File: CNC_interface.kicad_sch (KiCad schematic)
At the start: 27 parts, among them J1 Conn_01x04_Male, J10 Conn_01x08, J11 Conn_01x08, J12 Conn_01x08, J13 Conn_01x08, J14 Conn_01x03_Male, J15 Conn_01x03_Male, J16 Conn_01x03_Male, J17 Conn_01x08, J18 Conn_01x10, J19 USB_C_Receptacle, J2 Conn_01x04_Male, J3 Conn_01x04_Male, J5 Screw_Terminal_01x02, J6 Screw_Terminal_01x02, J8 Conn_01x08, J9 Conn_01x08, Q1 Q_NMOS_GDS, U4 LM2596S-5

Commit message: Starting routing & adding capa
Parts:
- added C3, C4, C5: C_Polarized, symbol Device:C_Polarized
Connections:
- net GND is gone; now on net +5V: C1.2, C2.2, D2.2 (A), J10.1 (Pin_1), J10.7 (Pin_7), J12.1 (Pin_1), J12.7 (Pin_7), J14.2 (Pin_2), J15.2 (Pin_2), J16.2 (Pin_2), J18.4 (Pin_4), J19.A1 (GND), J19.A12 (GND), J19.B1 (GND), J19.B12 (GND), J19.S1 (SHIELD), J5.2 (Pin_2), J8.1 (Pin_1), J8.7 (Pin_7), Q1.3 (S), R1.2, U4.3 (GND), U4.5 (~{ON}/OFF)
- net +5V: now also C3.1, C3.2, C4.1, C4.2, C5.1, C5.2
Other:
- moved on the sheet: J10, J11, J12, J13

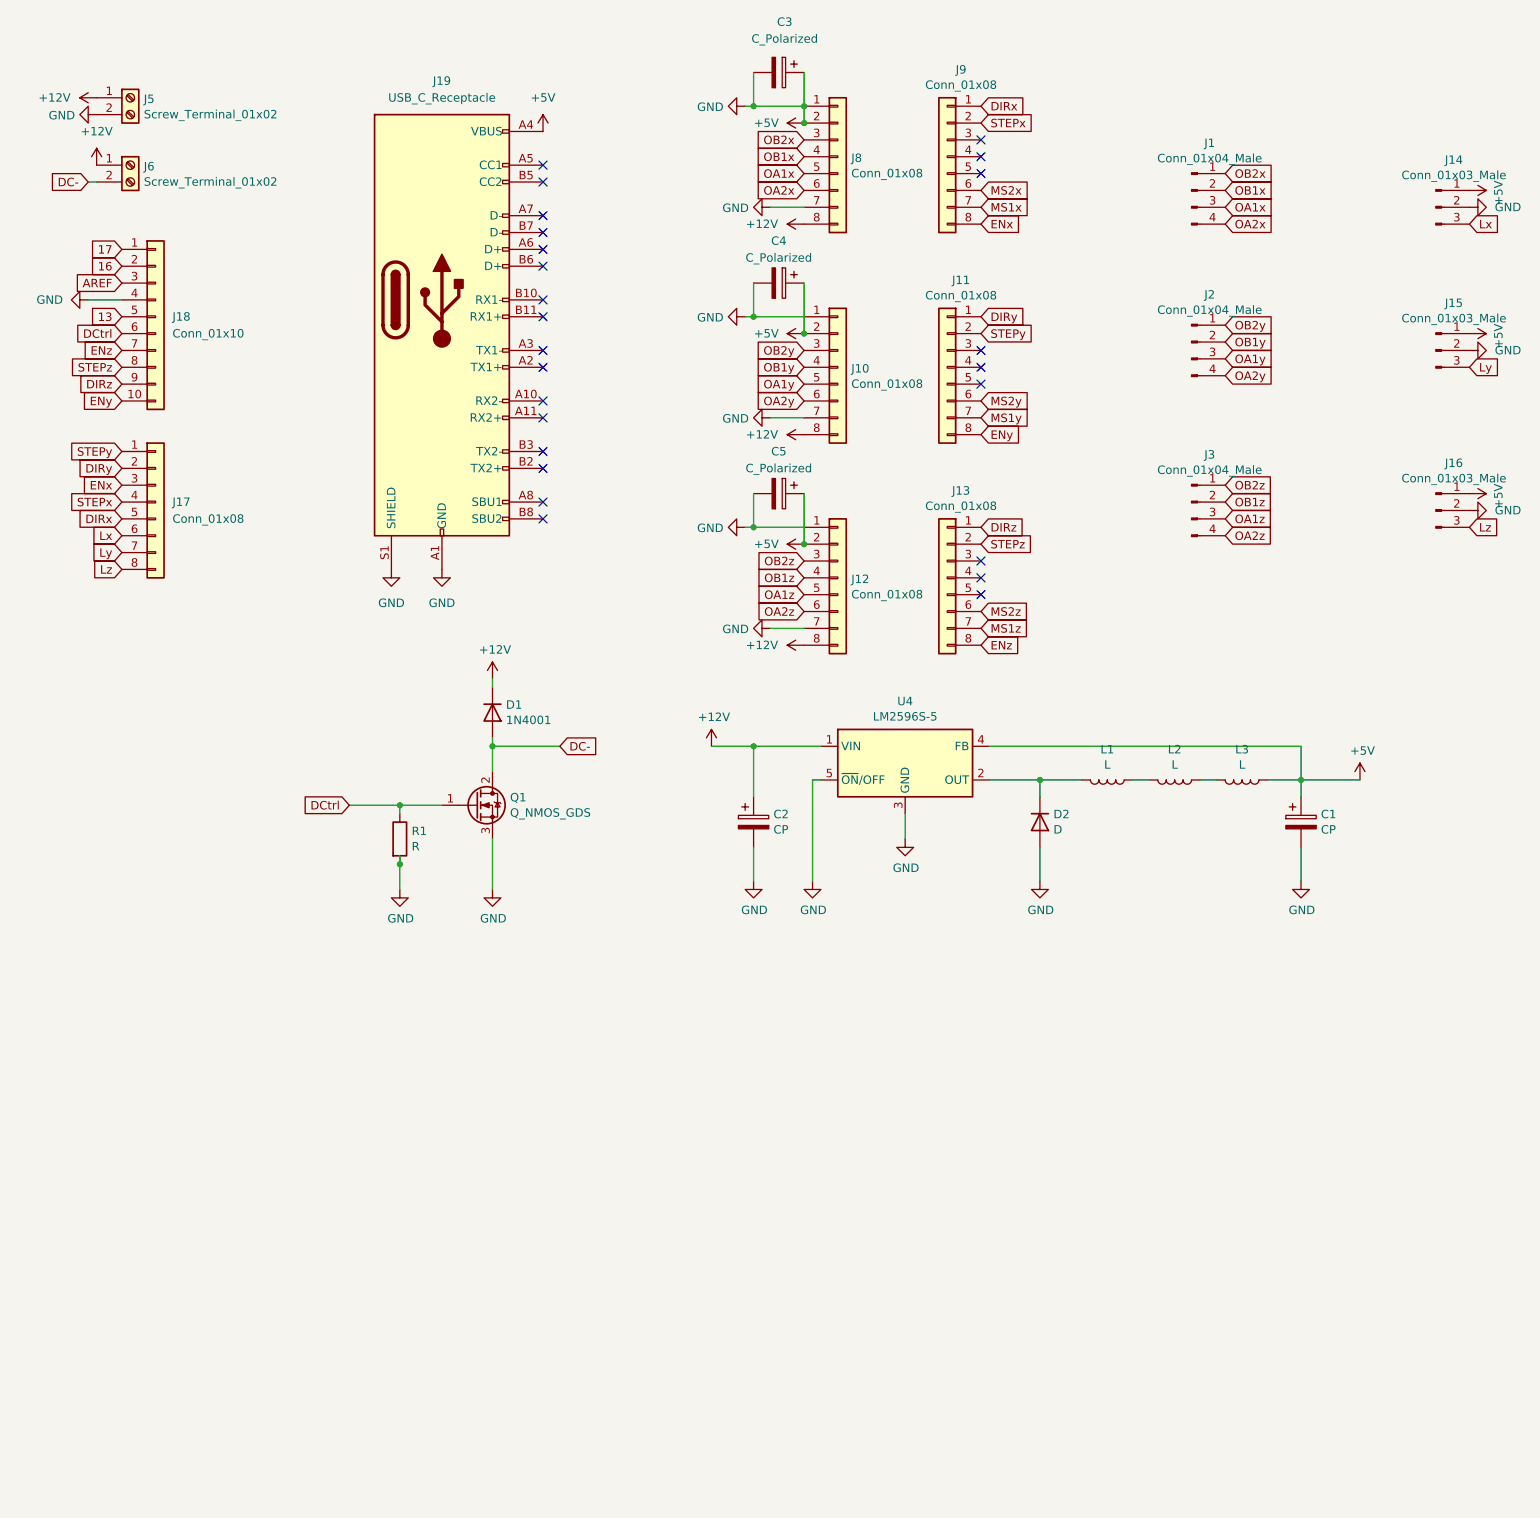
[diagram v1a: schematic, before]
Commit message: Add 12V power stage
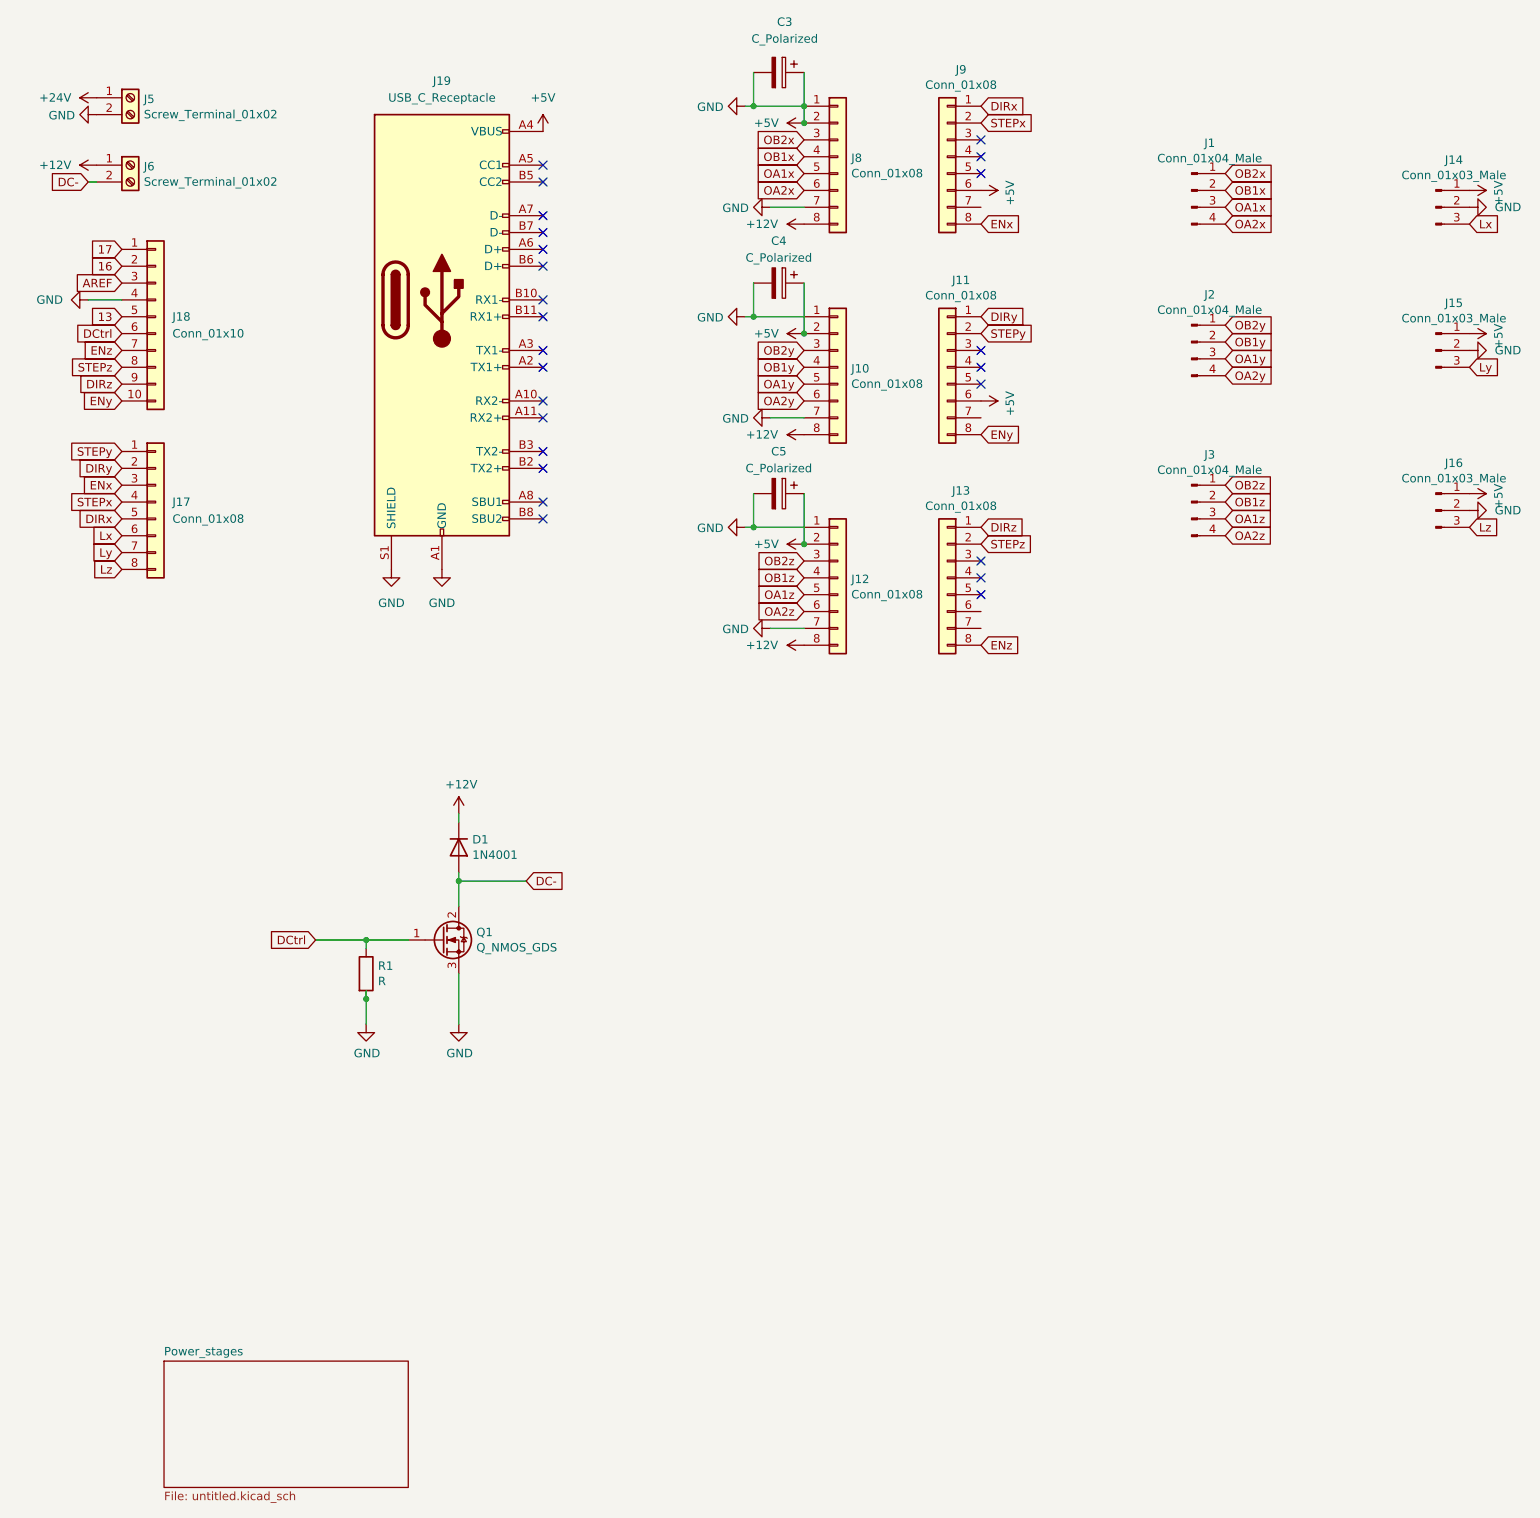
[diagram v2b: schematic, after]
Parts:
- removed C1: CP, Capacitor_THT:CP_Radial_D8.0mm_P3.50mm, symbol Device:CP
- removed C2: CP, Capacitor_THT:CP_Radial_D10.0mm_P5.00mm, symbol Device:CP
- removed D2: D, Diode_THT:D_DO-201AD_P15.24mm_Horizontal, symbol Device:D
- removed L1, L2, L3: L, Inductor_SMD:L_TDK_SLF10145, symbol Device:L
- removed U4: LM2596S-5, Package_TO_SOT_SMD:TO-263-5_TabPin3, symbol Regulator_Switching:LM2596S-5
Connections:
- net MS2x is gone; now on net +5V: J9.6 (Pin_6)
- net MS2y is gone; now on net +5V: J11.6 (Pin_6)
- net +12V: no longer J5.1 (Pin_1)
- net MS1x: no longer names the net of J9.7 (Pin_7)
- net MS1y: no longer names the net of J11.7 (Pin_7)
- net MS1z: no longer names the net of J13.7 (Pin_7)
- net MS2z: no longer names the net of J13.6 (Pin_6)
- new net +24V: J5.1 (Pin_1)
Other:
- added sheet Power_stages (untitled.kicad_sch)
- moved on the sheet: D1, Q1, R1

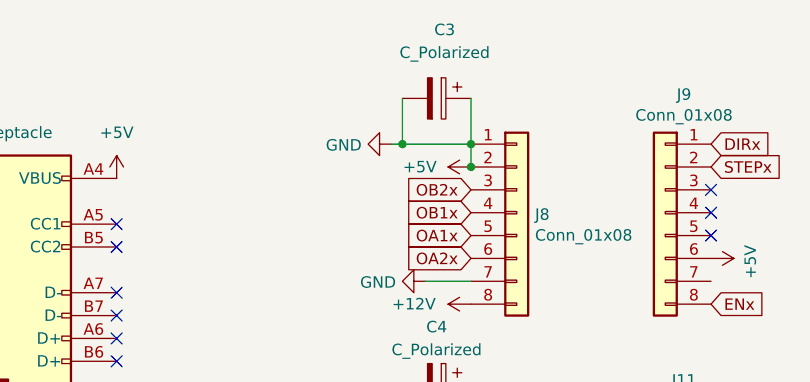
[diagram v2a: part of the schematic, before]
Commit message: delete the short circuit
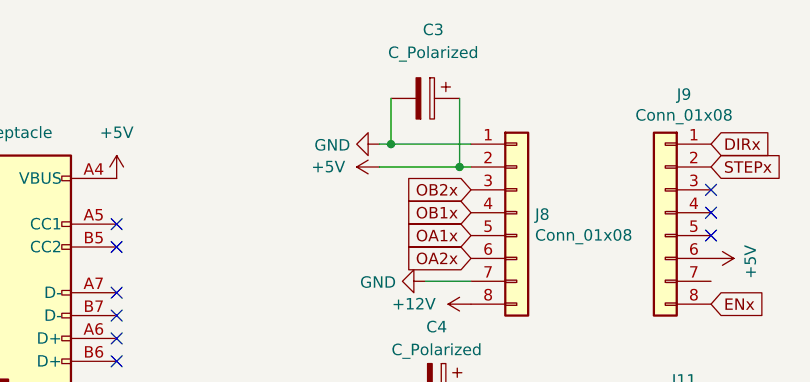
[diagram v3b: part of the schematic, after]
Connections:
- net +5V: no longer C3.2, C4.2, C5.2, J10.1 (Pin_1), J10.7 (Pin_7), J12.1 (Pin_1), J12.7 (Pin_7), J14.2 (Pin_2), J15.2 (Pin_2), J16.2 (Pin_2), J18.4 (Pin_4), J19.A1 (GND), J19.A12 (GND), J19.B1 (GND), J19.B12 (GND), J19.S1 (SHIELD), J5.2 (Pin_2), J8.1 (Pin_1), J8.7 (Pin_7), Q1.3 (S), R1.2
- new net GND: C3.2, C4.2, C5.2, J10.1 (Pin_1), J10.7 (Pin_7), J12.1 (Pin_1), J12.7 (Pin_7), J14.2 (Pin_2), J15.2 (Pin_2), J16.2 (Pin_2), J18.4 (Pin_4), J19.A1 (GND), J19.A12 (GND), J19.B1 (GND), J19.B12 (GND), J19.S1 (SHIELD), J5.2 (Pin_2), J8.1 (Pin_1), J8.7 (Pin_7), Q1.3 (S), R1.2
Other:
- moved on the sheet: C3
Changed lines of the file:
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@@
 (kicad_sch (version 20211123) (generator eeschema)
   (paper "A4")
-  (junction (at 148.59 35.56) (diameter 0) (color 0 0 0 0)
-  )
-  (junction (at 140.97 33.02) (diameter 0) (color 0 0 0 0)
-  )
   (junction (at 148.59 99.06) (diameter 0) (color 0 0 0 0)
   )
@@
   (junction (at 140.97 96.52) (diameter 0) (color 0 0 0 0)
   )
-  (junction (at 148.59 33.02) (diameter 0) (color 0 0 0 0)
+  (junction (at 147.32 35.56) (diameter 0) (color 0 0 0 0)
   )
   (junction (at 82.55 167.64) (diameter 0) (color 0 0 0 0)
+  )
+  (junction (at 139.7 33.02) (diameter 0) (color 0 0 0 0)
   )
   (no_connect (at 175.26 101.6))
@@
   (no_connect (at 109.22 49.53))
   (no_connect (at 109.22 44.45))
-  (wire (pts (xy 139.7 33.02) (xy 140.97 33.02))
+  (wire (pts (xy 138.43 33.02) (xy 139.7 33.02))
     (stroke (width 0) (type default) (color 0 0 0 0))
   )
@@
     (stroke (width 0) (type default) (color 0 0 0 0))
   )
-  (wire (pts (xy 140.97 27.94) (xy 140.97 33.02))
+  (wire (pts (xy 139.7 27.94) (xy 139.7 33.02))
     (stroke (width 0) (type default) (color 0 0 0 0))
   )
@@
     (stroke (width 0) (type default) (color 0 0 0 0))
   )
+  (wire (pts (xy 138.43 35.56) (xy 147.32 35.56))
+    (stroke (width 0) (type default) (color 0 0 0 0))
+  )
   (wire (pts (xy 106.68 149.86) (xy 96.52 149.86))
     (stroke (width 0) (type default) (color 0 0 0 0))
@@
     (stroke (width 0) (type default) (color 0 0 0 0))
   )
-  (wire (pts (xy 148.59 27.94) (xy 148.59 33.02))
-    (stroke (width 0) (type default) (color 0 0 0 0))
-  )
   (wire (pts (xy 140.97 59.69) (xy 140.97 64.77))
     (stroke (width 0) (type default) (color 0 0 0 0))
@@
     (stroke (width 0) (type default) (color 0 0 0 0))
   )
+  (wire (pts (xy 147.32 27.94) (xy 147.32 35.56))
+    (stroke (width 0) (type default) (color 0 0 0 0))
+  )
   (wire (pts (xy 140.97 91.44) (xy 140.97 96.52))
     (stroke (width 0) (type default) (color 0 0 0 0))
@@
     (stroke (width 0) (type default) (color 0 0 0 0))
   )
-  (wire (pts (xy 148.59 33.02) (xy 148.59 35.56))
-    (stroke (width 0) (type default) (color 0 0 0 0))
-  )
   (wire (pts (xy 40.64 62.23) (xy 45.72 62.23))
     (stroke (width 0) (type default) (color 0 0 0 0))
   )
+  (wire (pts (xy 139.7 33.02) (xy 148.59 33.02))
+    (stroke (width 0) (type default) (color 0 0 0 0))
+  )
+  (wire (pts (xy 147.32 35.56) (xy 148.59 35.56))
+    (stroke (width 0) (type default) (color 0 0 0 0))
+  )
   (wire (pts (xy 96.52 149.86) (xy 96.52 148.59))
     (stroke (width 0) (type default) (color 0 0 0 0))
@@
   )
   (wire (pts (xy 96.52 153.67) (xy 96.52 149.86))
-    (stroke (width 0) (type default) (color 0 0 0 0))
-  )
-  (wire (pts (xy 140.97 33.02) (xy 148.59 33.02))
     (stroke (width 0) (type default) (color 0 0 0 0))
   )
@@
     (pin "8")
   )
-  (symbol (lib_id "power:GND") (at 139.7 33.02 270) (unit 1)
-    (in_bom yes) (on_board yes)
-    (property "Reference" "#PWR0103" (id 0) (at 133.35 33.02 0)
-      (effects (font (size 1.27 1.27)) hide)
-    )
-    (property "Value" "GND" (id 1) (at 136.4488 33.147 90)
+  (symbol (lib_id "power:GND") (at 138.43 33.02 270) (unit 1)
+    (in_bom yes) (on_board yes)
+    (property "Reference" "#PWR0103" (id 0) (at 132.08 33.02 0)
+      (effects (font (size 1.27 1.27)) hide)
+    )
+    (property "Value" "GND" (id 1) (at 135.1788 33.147 90)
       (effects (font (size 1.27 1.27)) (justify right))
     )
-    (property "Footprint" "" (id 2) (at 139.7 33.02 0)
-      (effects (font (size 1.27 1.27)) hide)
-    )
-    (property "Datasheet" "" (id 3) (at 139.7 33.02 0)
+    (property "Footprint" "" (id 2) (at 138.43 33.02 0)
+      (effects (font (size 1.27 1.27)) hide)
+    )
+    (property "Datasheet" "" (id 3) (at 138.43 33.02 0)
       (effects (font (size 1.27 1.27)) hide)
     )
@@
     (pin "1")
   )
-  (symbol (lib_id "Device:C_Polarized") (at 144.78 27.94 270) (unit 1)
-    (in_bom yes) (on_board yes) (fields_autoplaced)
-    (property "Reference" "C3" (id 0) (at 145.669 20.32 90))
-    (property "Value" "C_Polarized" (id 1) (at 145.669 22.86 90))
-    (property "Footprint" "" (id 2) (at 140.97 28.9052 0)
-      (effects (font (size 1.27 1.27)) hide)
-    )
-    (property "Datasheet" "~" (id 3) (at 144.78 27.94 0)
+  (symbol (lib_id "Device:C_Polarized") (at 143.51 27.94 270) (unit 1)
+    (in_bom yes) (on_board yes) (fields_autoplaced)
+    (property "Reference" "C3" (id 0) (at 144.399 20.32 90))
+    (property "Value" "C_Polarized" (id 1) (at 144.399 22.86 90))
+    (property "Footprint" "" (id 2) (at 139.7 28.9052 0)
+      (effects (font (size 1.27 1.27)) hide)
+    )
+    (property "Datasheet" "~" (id 3) (at 143.51 27.94 0)
       (effects (font (size 1.27 1.27)) hide)
     )
@@
     (pin "2")
   )
-  (symbol (lib_id "power:+5V") (at 148.59 35.56 90) (unit 1)
-    (in_bom yes) (on_board yes) (fields_autoplaced)
-    (property "Reference" "#PWR0131" (id 0) (at 152.4 35.56 0)
-      (effects (font (size 1.27 1.27)) hide)
-    )
-    (property "Value" "+5V" (id 1) (at 144.78 35.5599 90)
-      (effects (font (size 1.27 1.27)) (justify left))
-    )
-    (property "Footprint" "" (id 2) (at 148.59 35.56 0)
-      (effects (font (size 1.27 1.27)) hide)
-    )
-    (property "Datasheet" "" (id 3) (at 148.59 35.56 0)
-      (effects (font (size 1.27 1.27)) hide)
-    )
+  (symbol (lib_id "power:+5V") (at 138.43 35.56 90) (unit 1)
+    (in_bom yes) (on_board yes) (fields_autoplaced)
+    (property "Reference" "#PWR0131" (id 0) (at 142.24 35.56 0)
+      (effects (font (size 1.27 1.27)) hide)
+    )
+    (property "Value" "+5V" (id 1) (at 134.62 35.5599 90)
+      (effects (font (size 1.27 1.27)) (justify left))
+    )
+    (property "Footprint" "" (id 2) (at 138.43 35.56 0)
+      (effects (font (size 1.27 1.27)) hide)
+    )
+    (property "Datasheet" "" (id 3) (at 138.43 35.56 0)
+      (effects (font (size 1.27 1.27)) hide)
+    )
